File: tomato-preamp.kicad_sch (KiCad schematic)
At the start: 25 parts, among them J1 IN, J2 OUT, J3.1 +ANODE, J3.2 -ANODE, J4.1 +HEATER, J4.2 -HEATER, U1 6N2P

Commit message: a slightly refined board
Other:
- title: (none) -> "Adjika" guitar preamp
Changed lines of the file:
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@@
 	(generator_version "9.0")
 	(paper "A4")
+	(title_block
+		(title "\"Adjika\" guitar preamp")
+	)
 	(junction
 		(at 101.6 100.33)

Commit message: intermittent
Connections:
- net High voltage: now reaches C6.1, R10.2, R7.2, U1.1 (A)
- net High voltage: now also C2.1, C2.2, C3.1, C4.2, C6.2, J3.1.1 (Pin_1), R10.1, R4.1, R4.2, R5.2, R7.1, R9.1, R9.2, RV1.2, RV2.1, U1.2 (G), U1.6 (A)
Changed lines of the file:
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@@
+		)
+	)
+	(label "High voltage"
+		(at 185.42 73.66 0)
+		(effects
+			(font
+				(size 1.27 1.27)
+			)
+			(justify left bottom)
+		)
+	)
+	(label "High voltage"
+		(at 120.65 69.85 270)
+		(effects
+			(font
+				(size 1.27 1.27)
+			)
+			(justify right bottom)
+		)
+	)
+	(label "High voltage"
+		(at 104.14 74.93 180)
+		(effects
+			(font
+				(size 1.27 1.27)
+			)
+			(justify right bottom)
+		)
+	)
+	(label "High voltage"
+		(at 167.64 74.93 0)
+		(effects
+			(font
+				(size 1.27 1.27)
+			)
+			(justify left bottom)
+		)
+	)
+	(label "High voltage"
+		(at 115.57 49.53 0)
+		(effects
+			(font
+				(size 1.27 1.27)
+			)
+			(justify left bottom)
+		)
+	)
+	(label "High voltage"
+		(at 157.48 83.82 90)
+		(effects
+			(font
+				(size 1.27 1.27)
+			)
+			(justify left bottom)
 		)
 	)

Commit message: update CBB capacitors footprints
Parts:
- C2, C6: footprint Capacitor_THT:C_Axial_L3.8mm_D2.6mm_P10.00mm_Horizontal -> Capacitor_THT:C_Rect_L11.0mm_W4.2mm_P10.00mm_MKT
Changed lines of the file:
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@@
 			)
 		)
-		(property "Footprint" "Capacitor_THT:C_Axial_L3.8mm_D2.6mm_P10.00mm_Horizontal"
+		(property "Footprint" "Capacitor_THT:C_Rect_L11.0mm_W4.2mm_P10.00mm_MKT"
 			(at 180.34 68.8848 0)
 			(effects
@@
 			)
 		)
-		(property "Footprint" "Capacitor_THT:C_Axial_L3.8mm_D2.6mm_P10.00mm_Horizontal"
+		(property "Footprint" "Capacitor_THT:C_Rect_L11.0mm_W4.2mm_P10.00mm_MKT"
 			(at 118.11 68.8848 0)
 			(effects

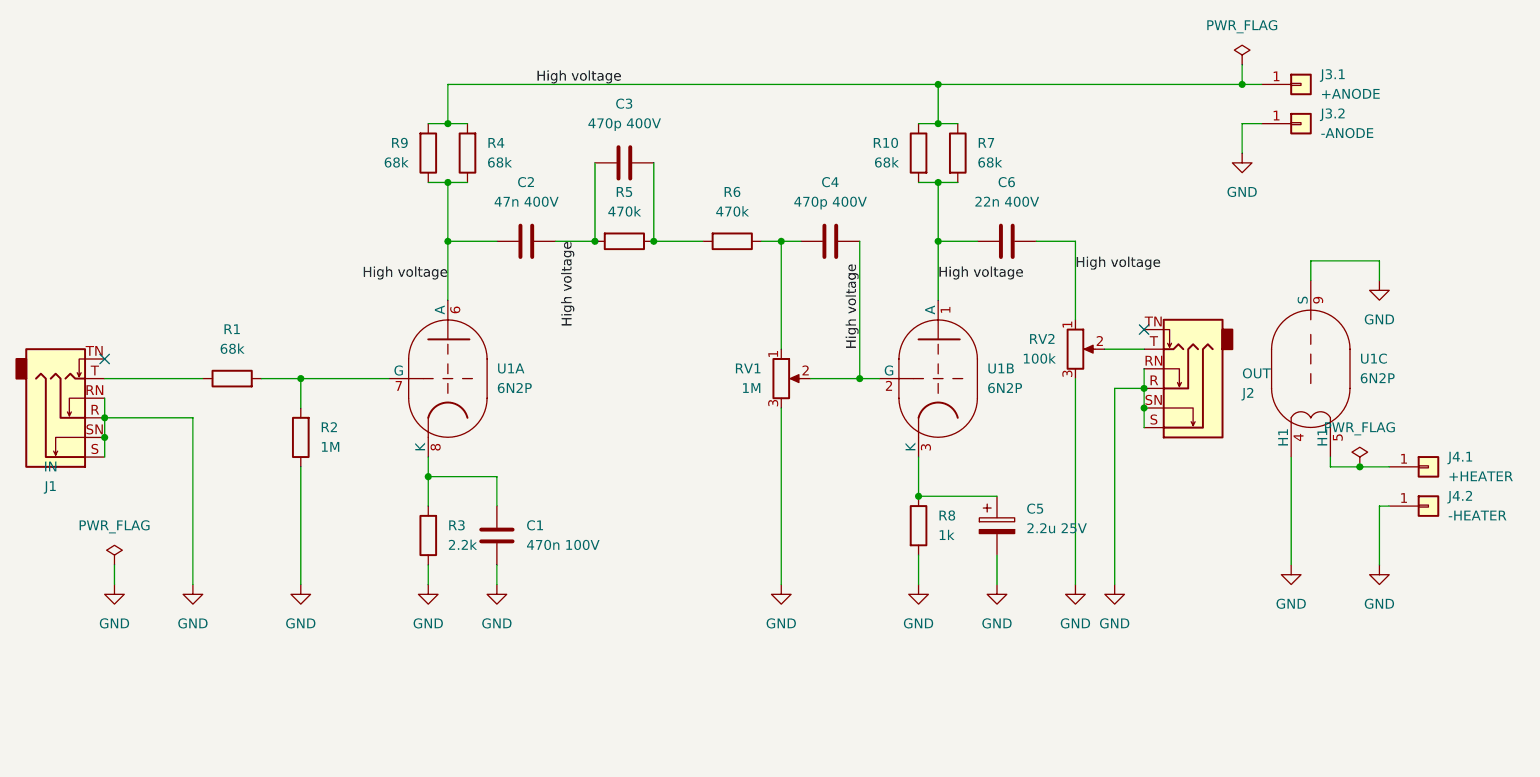
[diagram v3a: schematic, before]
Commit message: Update footprints
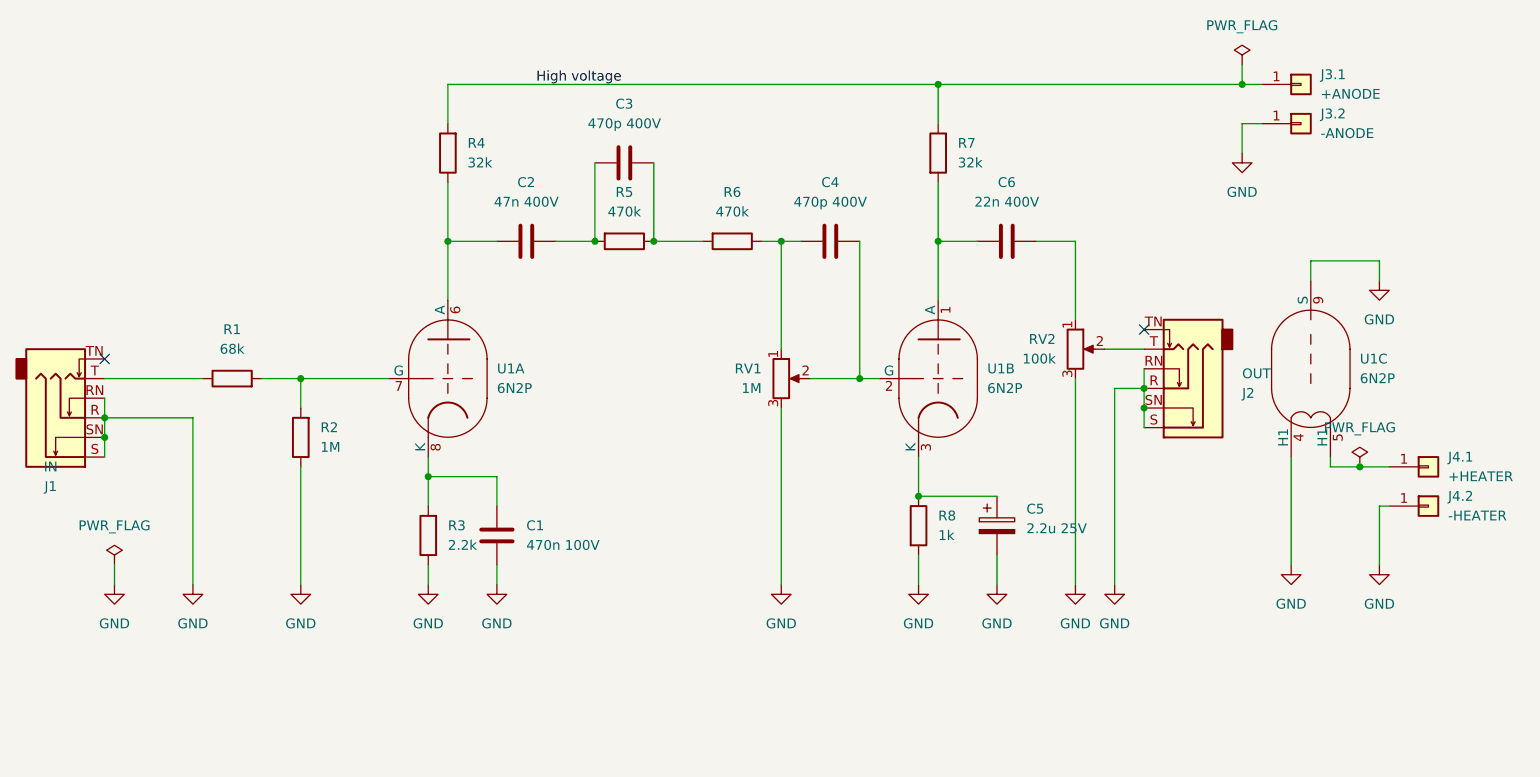
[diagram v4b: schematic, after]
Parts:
- removed R10, R9: 68k, Resistor_THT:R_Axial_DIN0207_L6.3mm_D2.5mm_P10.16mm_Horizontal, symbol Device:R
- R4, R7: value 68k -> 32k; footprint Resistor_THT:R_Axial_DIN0207_L6.3mm_D2.5mm_P10.16mm_Horizontal -> Resistor_THT:R_Axial_DIN0516_L15.5mm_D5.0mm_P20.32mm_Horizontal
- R5, R6: footprint Resistor_THT:R_Axial_DIN0207_L6.3mm_D2.5mm_P10.16mm_Horizontal -> Resistor_THT:R_Axial_DIN0516_L15.5mm_D5.0mm_P20.32mm_Horizontal
- U1: footprint Valve:Valve_Noval_P -> tubes:Valve_6N2P-3
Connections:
- net High voltage: no longer C2.1, C2.2, C3.1, C4.2, C6.1, C6.2, R4.1, R5.2, R7.2, RV1.2, RV2.1, U1.1 (A), U1.2 (G), U1.6 (A)
- new net: C6.1, R7.2, U1.1 (A)
- new net: C4.2, RV1.2, U1.2 (G)
- new net: C6.2, RV2.1
- new net: C2.2, C3.1, R5.2
- new net: C2.1, R4.1, U1.6 (A)
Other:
- moved on the sheet: R4, R7

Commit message: Add modifications to the schematic
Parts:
- added C7, C8: 22u 400V, symbol Device:C_Polarized
- added R10, R11, R12, R9: 1K, symbol Device:R
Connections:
- net GND: now also C7.2, C8.2, R11.2, R12.2; no longer RV1.3, RV2.3
- net High voltage: now also C8.1, R10.1; no longer J3.1.1 (Pin_1), R7.1
- new net: C7.1, R10.2, R7.1, R9.1
- new net: R11.1, RV2.3
- new net: R12.1, RV1.3
- new net: J3.1.1 (Pin_1), R9.2

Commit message: Temp
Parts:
- C7: footprint (none) -> Capacitor_THT:CP_Radial_D13.0mm_P7.50mm\
- C8: footprint (none) -> Capacitor_THT:CP_Radial_D13.0mm_P7.50mm

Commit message: Rewire
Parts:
- C7: footprint Capacitor_THT:CP_Radial_D13.0mm_P7.50mm\ -> Capacitor_THT:CP_Radial_D13.0mm_P7.50mm
- R10, R9: value 1K -> 1K 2W; footprint (none) -> Resistor_THT:R_Axial_DIN0516_L15.5mm_D5.0mm_P20.32mm_Horizontal
- R11, R12: footprint (none) -> Resistor_THT:R_Axial_DIN0207_L6.3mm_D2.5mm_P10.16mm_Horizontal
- R4, R7: value 32k -> 32k 2W
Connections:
- net High voltage: no longer names the net of C8.1, R10.1, R4.2
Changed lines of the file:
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@@
 		)
 	)
-	(label "High voltage"
-		(at 115.57 49.53 0)
-		(effects
-			(font
-				(size 1.27 1.27)
-			)
-			(justify left bottom)
-		)
-	)
 	(symbol
 		(lib_id "Device:R")
@@
 			)
 		)
-		(property "Value" "1K"
+		(property "Value" "1K 2W"
 			(at 152.4 45.72 90)
 			(show_name no)
@@
 			)
 		)
-		(property "Footprint" ""
+		(property "Footprint" "Resistor_THT:R_Axial_DIN0516_L15.5mm_D5.0mm_P20.32mm_Horizontal"
 			(at 152.4 51.308 90)
 			(hide yes)
@@
 			)
 		)
-		(property "Value" "32k"
+		(property "Value" "32k 2W"
 			(at 170.18 59.6899 0)
 			(show_name no)
@@
 			)
 		)
-		(property "Value" "32k"
+		(property "Value" "32k 2W"
 			(at 106.68 59.6899 0)
 			(show_name no)
@@
 			)
 		)
-		(property "Footprint" ""
+		(property "Footprint" "Resistor_THT:R_Axial_DIN0207_L6.3mm_D2.5mm_P10.16mm_Horizontal"
 			(at 145.542 100.33 90)
 			(hide yes)
@@
 			)
 		)
-		(property "Footprint" ""
+		(property "Footprint" "Resistor_THT:R_Axial_DIN0207_L6.3mm_D2.5mm_P10.16mm_Horizontal"
 			(at 183.642 97.79 90)
 			(hide yes)
@@
 			)
 		)
-		(property "Footprint" "Capacitor_THT:CP_Radial_D13.0mm_P7.50mm\\"
+		(property "Footprint" "Capacitor_THT:CP_Radial_D13.0mm_P7.50mm"
 			(at 188.9252 58.42 0)
 			(hide yes)
@@
 			)
 		)
-		(property "Value" "1K"
+		(property "Value" "1K 2W"
 			(at 194.31 45.72 90)
 			(show_name no)
@@
 			)
 		)
-		(property "Footprint" ""
+		(property "Footprint" "Resistor_THT:R_Axial_DIN0516_L15.5mm_D5.0mm_P20.32mm_Horizontal"
 			(at 194.31 51.308 90)
 			(hide yes)

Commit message: Update footprints
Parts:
- removed J3.1: +ANODE, TestPoint:TestPoint_THTPad_2.0x2.0mm_Drill1.0mm, symbol Connector_Generic:Conn_01x01
- removed J3.2: -ANODE, TestPoint:TestPoint_THTPad_2.0x2.0mm_Drill1.0mm, symbol Connector_Generic:Conn_01x01
- removed J4.1: +HEATER, TestPoint:TestPoint_THTPad_2.0x2.0mm_Drill1.0mm, symbol Connector_Generic:Conn_01x01
- removed J4.2: -HEATER, TestPoint:TestPoint_THTPad_2.0x2.0mm_Drill1.0mm, symbol Connector_Generic:Conn_01x01
- added J3: 200V, Connector_Wire:SolderWire-0.75sqmm_1x02_P7mm_D1.25mm_OD3.5mm, symbol Connector:Screw_Terminal_01x02
- added J4: 6V3, Connector_Wire:SolderWire-0.75sqmm_1x02_P7mm_D1.25mm_OD3.5mm, symbol Connector:Screw_Terminal_01x02
- added J5: GAIN_GND, Connector_Wire:SolderWire-0.127sqmm_1x01_D0.48mm_OD1mm, symbol Connector:Screw_Terminal_01x01
- added J6: VOL_GND, Connector_Wire:SolderWire-0.127sqmm_1x01_D0.48mm_OD1mm, symbol Connector:Screw_Terminal_01x01
- C1: footprint Capacitor_THT:C_Axial_L3.8mm_D2.6mm_P7.50mm_Horizontal -> Capacitor_THT:C_Rect_L7.2mm_W5.0mm_P5.00mm
- C2: footprint Capacitor_THT:C_Rect_L11.0mm_W4.2mm_P10.00mm_MKT -> Capacitor_THT:C_Rect_L11.0mm_W5.1mm_P10.00mm_MKT
- C3, C4: footprint Capacitor_THT:C_Axial_L3.8mm_D2.6mm_P10.00mm_Horizontal -> Capacitor_THT:C_Rect_L7.0mm_W3.5mm_P5.00mm
- C7, C8: footprint Capacitor_THT:CP_Radial_D13.0mm_P7.50mm -> Capacitor_THT:CP_Radial_D13.0mm_P5.00mm
- R5, R6: footprint Resistor_THT:R_Axial_DIN0516_L15.5mm_D5.0mm_P20.32mm_Horizontal -> Resistor_THT:R_Axial_DIN0207_L6.3mm_D2.5mm_P10.16mm_Horizontal
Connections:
- net GND: now also J1.TN, J2.TN, J3.2 (Pin_2), J5.1 (Pin_1), J6.1 (Pin_1); no longer U1.4 (H1)
- net at U1.5 (H1): now also J4.1 (Pin_1)
- net at R9.2: now also J3.1 (Pin_1)
- new net: J4.2 (Pin_2), U1.4 (H1)
- no-connect marks 2 -> 0
